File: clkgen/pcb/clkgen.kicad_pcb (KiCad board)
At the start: 2 copper layers, 14 x 104.1 mm, 21 parts, among them J1 AudioJack2_SwitchT, J2 AudioJack2_SwitchT, J3 AudioJack2_SwitchT, J4 AudioJack2_SwitchT, J5 AudioJack2_SwitchT, J6 EurorackPwr, U1 4521

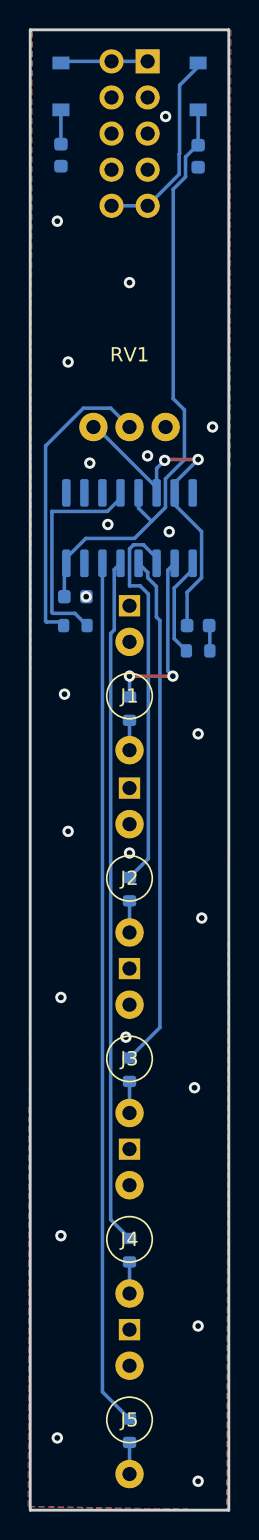
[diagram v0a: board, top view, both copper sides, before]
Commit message: rotated power connector ; added markings
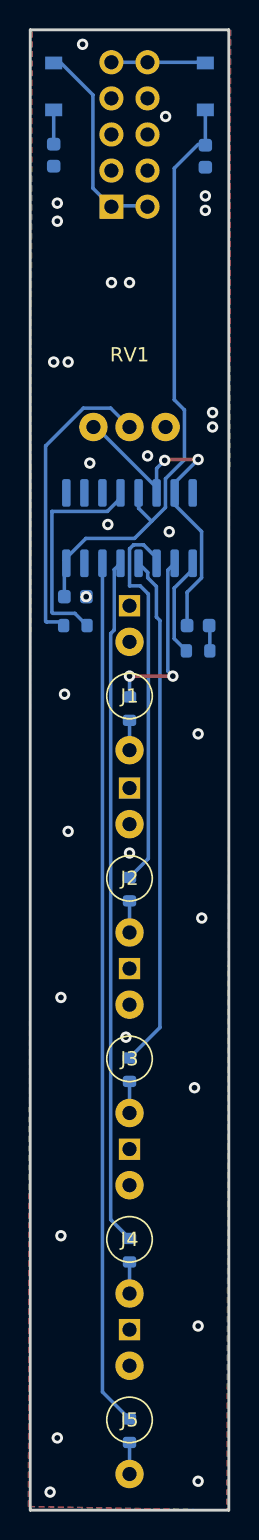
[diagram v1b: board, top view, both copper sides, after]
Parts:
- added G***: LOGO, eurorack_footprints:musikbeton_8mm_front, B.Cu at (63.5, 82.5)
- moved J6 10.5 mm to (62.2, 70.9), turned to 0 degrees
- moved C3 0.51 mm to (68.8, 67.3)
- moved D1 0.51 mm to (68.8, 62.4)
- moved C4 0.51 mm to (58.2, 67.2)
- moved D2 0.51 mm to (58.2, 62.4)
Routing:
- net Net-(D2-Pad2): track 6.15 -> 14.1 mm
- net Net-(D1-Pad2): track 13.8 -> 6.12 mm
- net GND: vias 22 -> 30
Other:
- board text added: "MB20220606"
- board text added: "RoHS"
- board text added: "red line"

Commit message: updated layout
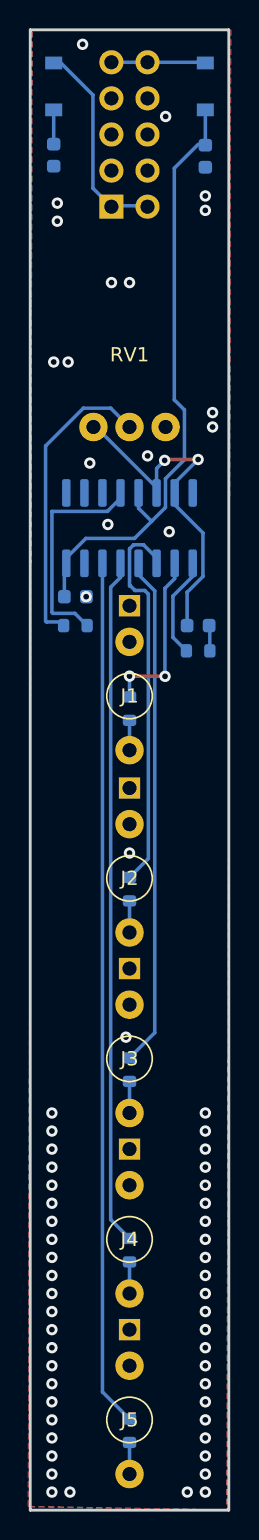
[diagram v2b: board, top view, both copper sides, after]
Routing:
- net Net-(R5-Pad1): track 12.8 -> 12.2 mm
- net GND: vias 30 -> 65
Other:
- board text added: "-12V (red)"
- board text removed: "MB20220606"
- board text removed: "red line"
